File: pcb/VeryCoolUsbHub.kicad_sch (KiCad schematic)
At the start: 10 parts, among them U1 HC-USB3.0-L168-WP, U2 RTL8152B-VB-CG, U3 GL3510-OSY52, U4 HC-USB3.0-L168-WP

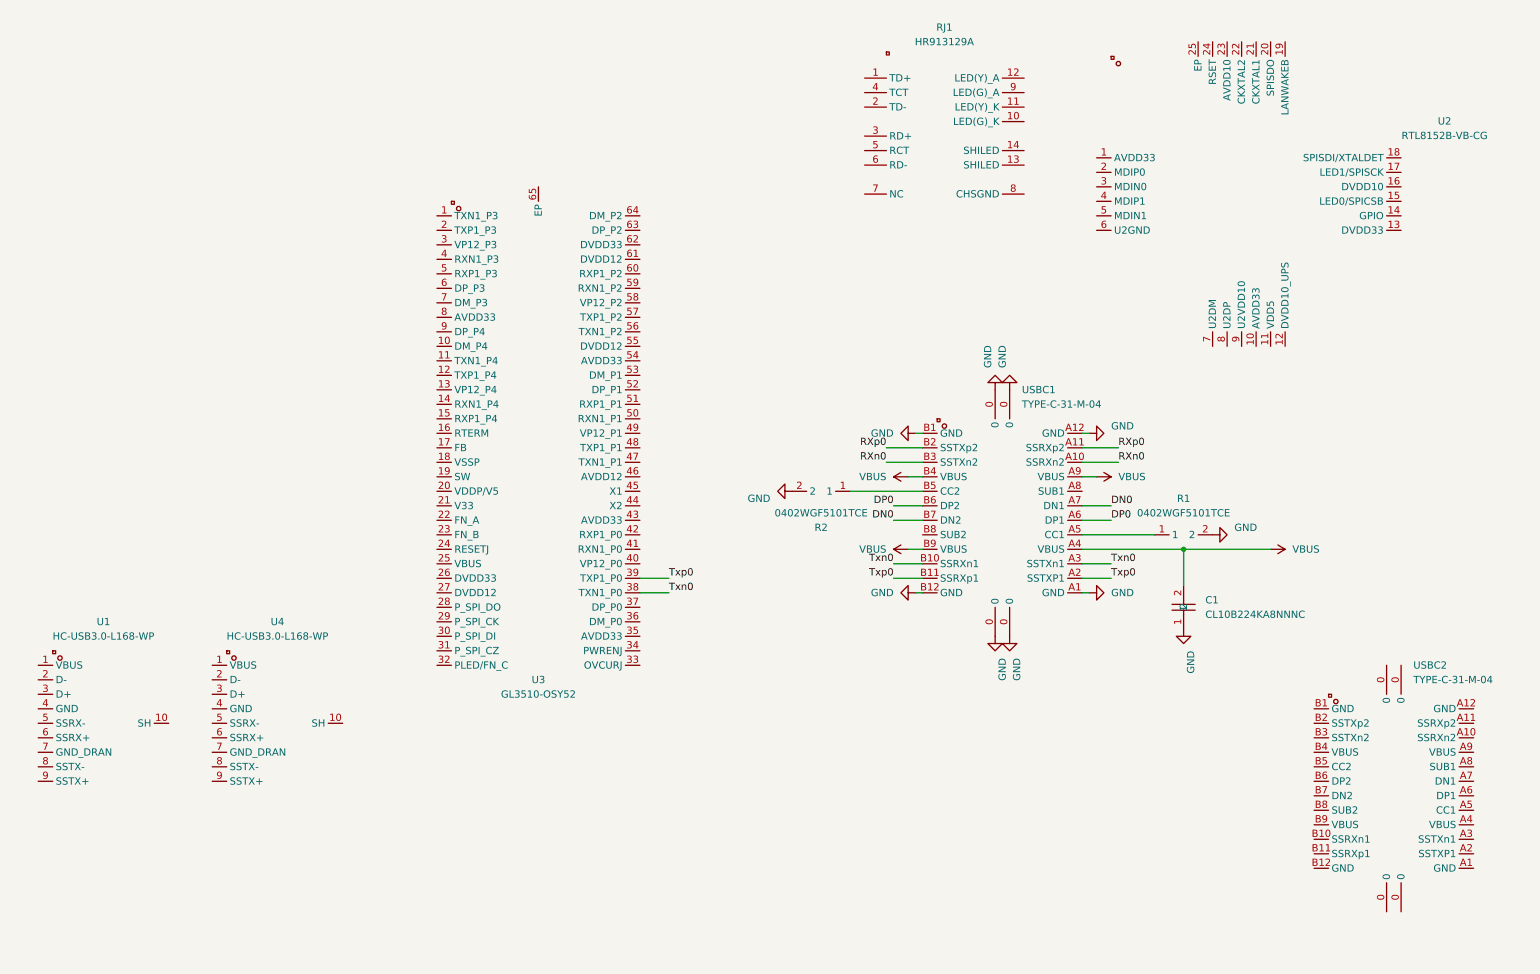
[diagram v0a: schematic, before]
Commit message: changed stuff, add schem for review
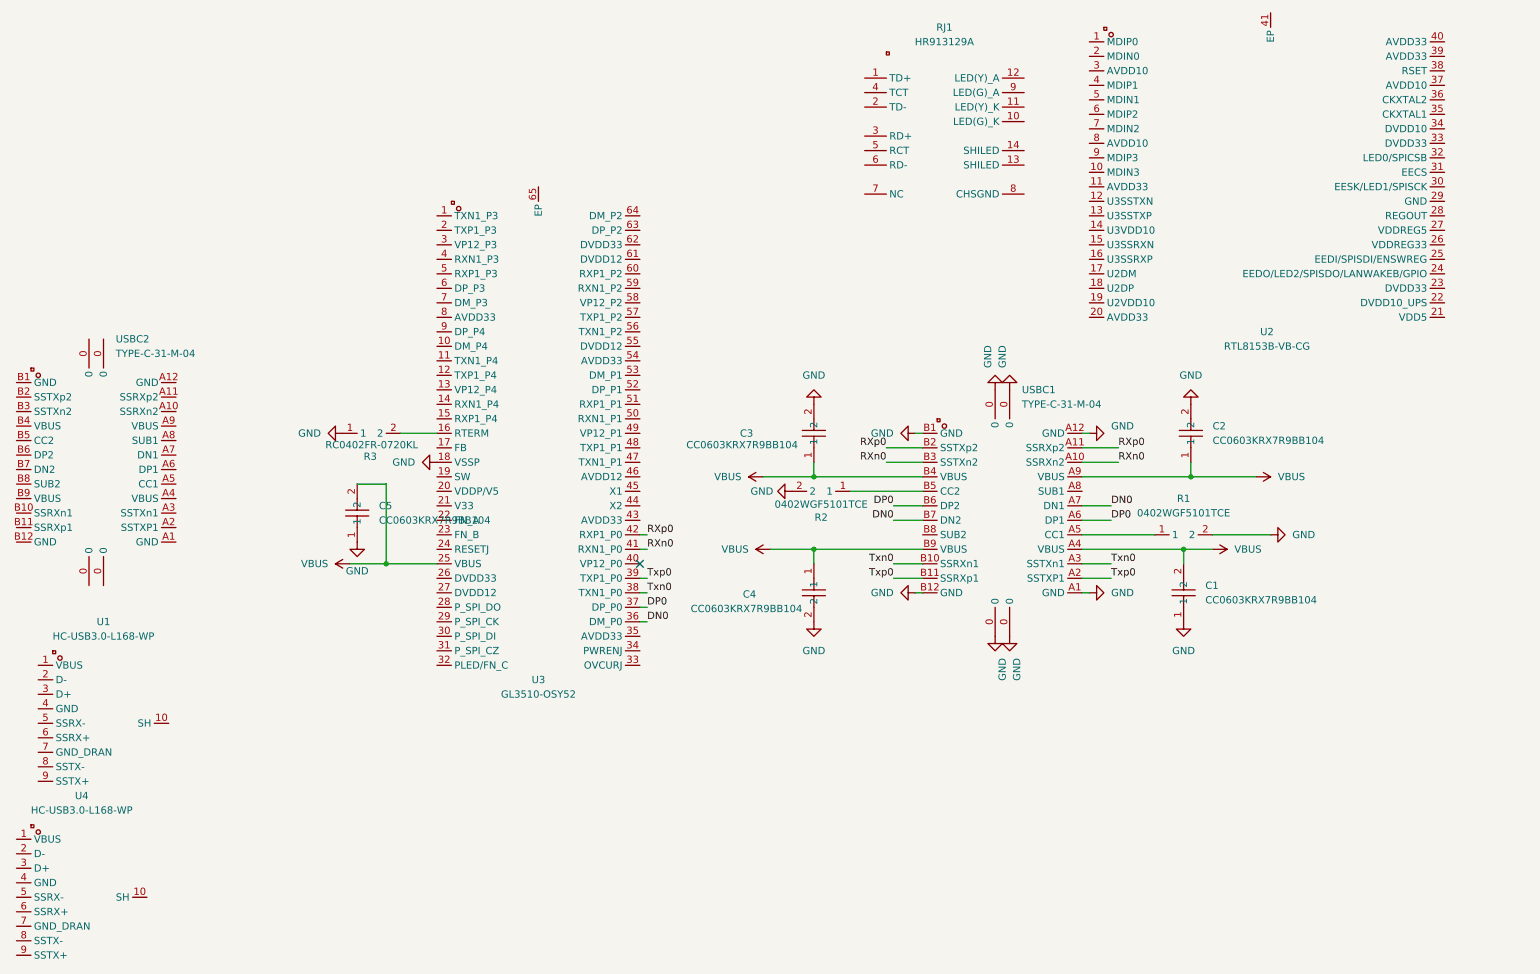
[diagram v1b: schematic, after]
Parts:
- removed C1: CL10B224KA8NNNC, EasyEDA:C0603, symbol EasyEDA:CL10B224KA8NNNC
- removed U2: RTL8152B-VB-CG, EasyEDA:QFN-24_L4.0-W4.0-P0.50-BL-EP2.0, symbol EasyEDA:RTL8152B-VB-CG
- added C1, C2, C3, C4, C5: CC0603KRX7R9BB104, EasyEDA:C0603, symbol EasyEDA:CC0603KRX7R9BB104
- added R3: RC0402FR-0720KL, EasyEDA:R0402, symbol EasyEDA:RC0402FR-0720KL
- added U2: RTL8153B-VB-CG, EasyEDA:QFN-40_L5.0-W5.0-P0.40-BL-EP3.7, symbol EasyEDA:RTL8153B-VB-CG
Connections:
- net DN0: now also U3.36 (DM_P0)
- net DP0: now also U3.37 (DP_P0)
- net GND: now also U3.18 (VSSP), C1.1, C2.2, C3.2, C4.2, C5.1, R3.1
- net RXn0: now also U3.41 (RXN1_P0)
- net RXp0: now also U3.42 (RXP1_P0)
- net VBUS: now also U3.25 (VBUS), C1.2, C2.1, C3.1, C4.1, C5.2
- net at U3.16 (RTERM): now also R3.2
- no-connect marks 0 -> 1
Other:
- moved on the sheet: U4, USBC2

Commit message: now with everything ig?
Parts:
- added C10, C11: CC0603KRX7R9BB104, EasyEDA:C0603, symbol EasyEDA:CC0603KRX7R9BB104
- added C6, C7: CC0603JRNPO9BN390, EasyEDA:C0603, symbol EasyEDA:CC0603JRNPO9BN390
- added C9: CL10A106KP8NNNC, EasyEDA:C0603, symbol EasyEDA:CL10A106KP8NNNC
- added X1: X322525MSB4SI, EasyEDA:CRYSTAL-SMD_4P-L3.2-W2.5-BL-2, symbol EasyEDA:X322525MSB4SI
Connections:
- net GND: now also C5.2, U1.10 (SH), U1.4 (GND), U1.7 (GND_DRAN), U4.10 (SH), U4.4 (GND), U4.7 (GND_DRAN), USBC2.0, USBC2.A1 (GND), USBC2.A12 (GND), USBC2.B1 (GND), USBC2.B12 (GND), C10.2, C11.2, C6.1, C7.2, C9.2, X1.2 (GND), X1.4 (GND); no longer C5.1
- net VBUS: now also C5.1, U1.1 (VBUS), U4.1 (VBUS), C10.1, C11.1, C9.1; no longer C5.2
- net at U2.35 (CKXTAL1): now also C6.2, X1.1 (OSC1)
- net at U2.36 (CKXTAL2): now also C7.1, X1.3 (OSC2)
- net DN1: now reaches U1.2 (D-)
- net DN1: now also U3.53 (DM_P1)
- net DP1: now reaches U1.3 (D+)
- net DP1: now also U3.52 (DP_P1)
- net RXn1: now reaches U1.5 (SSRX-)
- net RXn1: now also U3.50 (RXN1_P1)
- net RXp1: now reaches U1.6 (SSRX+)
- net RXp1: now also U3.51 (RXP1_P1)
- net Txn1: now reaches U1.8 (SSTX-)
- net Txn1: now also U3.47 (TXN1_P1)
- net Txp1: now reaches U1.9 (SSTX+)
- net Txp1: now also U3.48 (TXP1_P1)
- net Txn3: now reaches U3.1 (TXN1_P3)
- net Txp3: now reaches U3.2 (TXP1_P3)
- net RXn3: now reaches U3.4 (RXN1_P3)
- net RXp3: now reaches U3.5 (RXP1_P3)
- net Txn2: now reaches U3.56 (TXN1_P2)
- net Txn2: now also U4.8 (SSTX-)
- net Txp2: now reaches U3.57 (TXP1_P2)
- net Txp2: now also U4.9 (SSTX+)
- net RXn2: now reaches U3.59 (RXN1_P2)
- net RXn2: now also U4.5 (SSRX-)
- net DP3: now reaches U3.6 (DP_P3)
- net RXp2: now reaches U3.60 (RXP1_P2)
- net RXp2: now also U4.6 (SSRX+)
- net DP2: now reaches U3.63 (DP_P2)
- net DP2: now also U4.3 (D+)
- net DN2: now reaches U3.64 (DM_P2)
- net DN2: now also U4.2 (D-)
- net DN3: now reaches U3.7 (DM_P3)
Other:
- moved on the sheet: C1, C2, C3, C4, C5, R1, R2, RJ1, U1, U2, U4, USBC1

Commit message: done schem please
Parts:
- removed RJ1: HR913129A, EasyEDA:RJ45-TH_HR913129A, symbol EasyEDA:HR913129A
- added C12, C13, C14, C15, C16, C17, C8: CC0603KRX7R9BB104, EasyEDA:C0603, symbol EasyEDA:CC0603KRX7R9BB104
- added C18: CC0603JRNPO9BN390, EasyEDA:C0603, symbol EasyEDA:CC0603JRNPO9BN390
- added R4, R5: 0402WGF5602TCE, EasyEDA:R0402, symbol EasyEDA:0402WGF5602TCE
- added R6: RC0402FR-071KL, EasyEDA:R0402, symbol EasyEDA:RC0402FR-071KL
- added RJ45: HR911130A, EasyEDA:RJ45-TH_HR911130A, symbol EasyEDA:HR911130A
- added X2: X322525MSB4SI, EasyEDA:CRYSTAL-SMD_4P-L3.2-W2.5-BL-2, symbol EasyEDA:X322525MSB4SI
- renumbered USBC1 to USBC_IN, USBC2 to USBC_OUT, U1 to USB_OUT1, U4 to USB_OUT2
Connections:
- net DN3: now also U2.17 (U2DM), USBC_OUT.A7 (DN1)
- net DP3: now also USBC_OUT.A6 (DP1)
- net GND: now also C1.2, C2.1, C4.1, R1.1, U2.29 (GND), C12.1, C13.2, C14.1, C15.1, C16.2, C17.2, C18.1, C8.2, X2.2 (GND), X2.4 (GND); no longer C1.1, C2.2, C4.2, R1.2, USBC_IN.0, USBC_OUT.0, USB_OUT1.10 (SH), USB_OUT2.10 (SH)
- net RXn0: now also USBC_IN.B10 (SSRXn1); no longer USBC_IN.B3 (SSTXn2)
- net RXn3: now also USBC_OUT.A10 (SSRXn2)
- net RXp0: now also USBC_IN.B11 (SSRXp1); no longer USBC_IN.B2 (SSTXp2)
- net RXp3: now also USBC_OUT.A11 (SSRXp2)
- net Txn0: now also USBC_IN.B3 (SSTXn2); no longer USBC_IN.B10 (SSRXn1)
- net Txn3: now also USBC_OUT.A3 (SSTXn1)
- net Txp0: now also USBC_IN.B2 (SSTXp2); no longer USBC_IN.B11 (SSRXp1)
- net Txp3: now also USBC_OUT.A2 (SSTXP1)
- net VBUS: now also C1.1, C2.2, C4.2, U2.21 (VDD5), U2.27 (VDDREG5), U3.20 (VDDP/V5), USBC_OUT.A9 (VBUS), C13.1, C16.1, C17.1, C8.1, R4.2, R5.2; no longer C1.2, C2.1, C4.1
- net MDIP0: now reaches U2.1 (MDIP0)
- net MDIP0: now also RJ45.P2 (MDI0+)
- net MDIN3: now reaches U2.10 (MDIN3)
- net MDIN3: now also RJ45.P9 (MDI3-)
- net Txn4: now reaches U2.12 (U3SSTXN)
- net Txn4: now also U3.11 (TXN1_P4)
- net Txp4: now reaches U2.13 (U3SSTXP)
- net Txp4: now also U3.12 (TXP1_P4)
- net RXn4: now reaches U2.15 (U3SSRXN)
- net RXn4: now also U3.14 (RXN1_P4)
- net RXp4: now reaches U2.16 (U3SSRXP)
- net RXp4: now also U3.15 (RXP1_P4)
- net DP4: now reaches U2.18 (U2DP)
- net DP4: now also U3.9 (DP_P4)
- net MDIN0: now reaches U2.2 (MDIN0)
- net MDIN0: now also RJ45.P3 (MDI0-)
- net V3.3: now reaches U2.23 (DVDD33)
- net V3.3: now also U2.26 (VDDREG33), U3.21 (V33), C14.2, C15.2, R6.2
- net LED2: now reaches U2.24 (EEDO/LED2/SPISDO/LANWAKEB/GPIO)
- net LED2: now also RJ45.13
- net LED1: now reaches U2.30 (EESK/LED1/SPISCK)
- net LED1: now also RJ45.12
- net MDIP1: now reaches U2.4 (MDIP1)
- net MDIP1: now also RJ45.P4 (MDI1+)
- net MDIN1: now reaches U2.5 (MDIN1)
- net MDIN1: now also RJ45.P7 (MDI1-)
- net MDIP2: now reaches U2.6 (MDIP2)
- net MDIP2: now also RJ45.P5 (MDI2+)
- net MDIN2: now reaches U2.7 (MDIN2)
- net MDIN2: now also RJ45.P6 (MDI2-)
- net MDIP3: now reaches U2.9 (MDIP3)
- net MDIP3: now also RJ45.P8 (MDI3+)
- net at USBC_IN.A5 (CC1): now also R1.2; no longer R1.1
- net DN4: now reaches U3.10 (DM_P4)
- net at U3.44 (X2): now also C18.2, X2.3 (OSC2)
- net at U3.45 (X1): now also X2.1 (OSC1)
- net at USBC_OUT.A5 (CC1): now also R4.1
- net at USBC_OUT.B5 (CC2): now also R5.1
- new net: C12.2, RJ45.P1
- new net: R6.1, RJ45.11, RJ45.14
- no-connect marks 1 -> 40
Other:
- moved on the sheet: C1, C10, C11, C2, C3, C4, C5, C6, C7, C9, R1, R2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

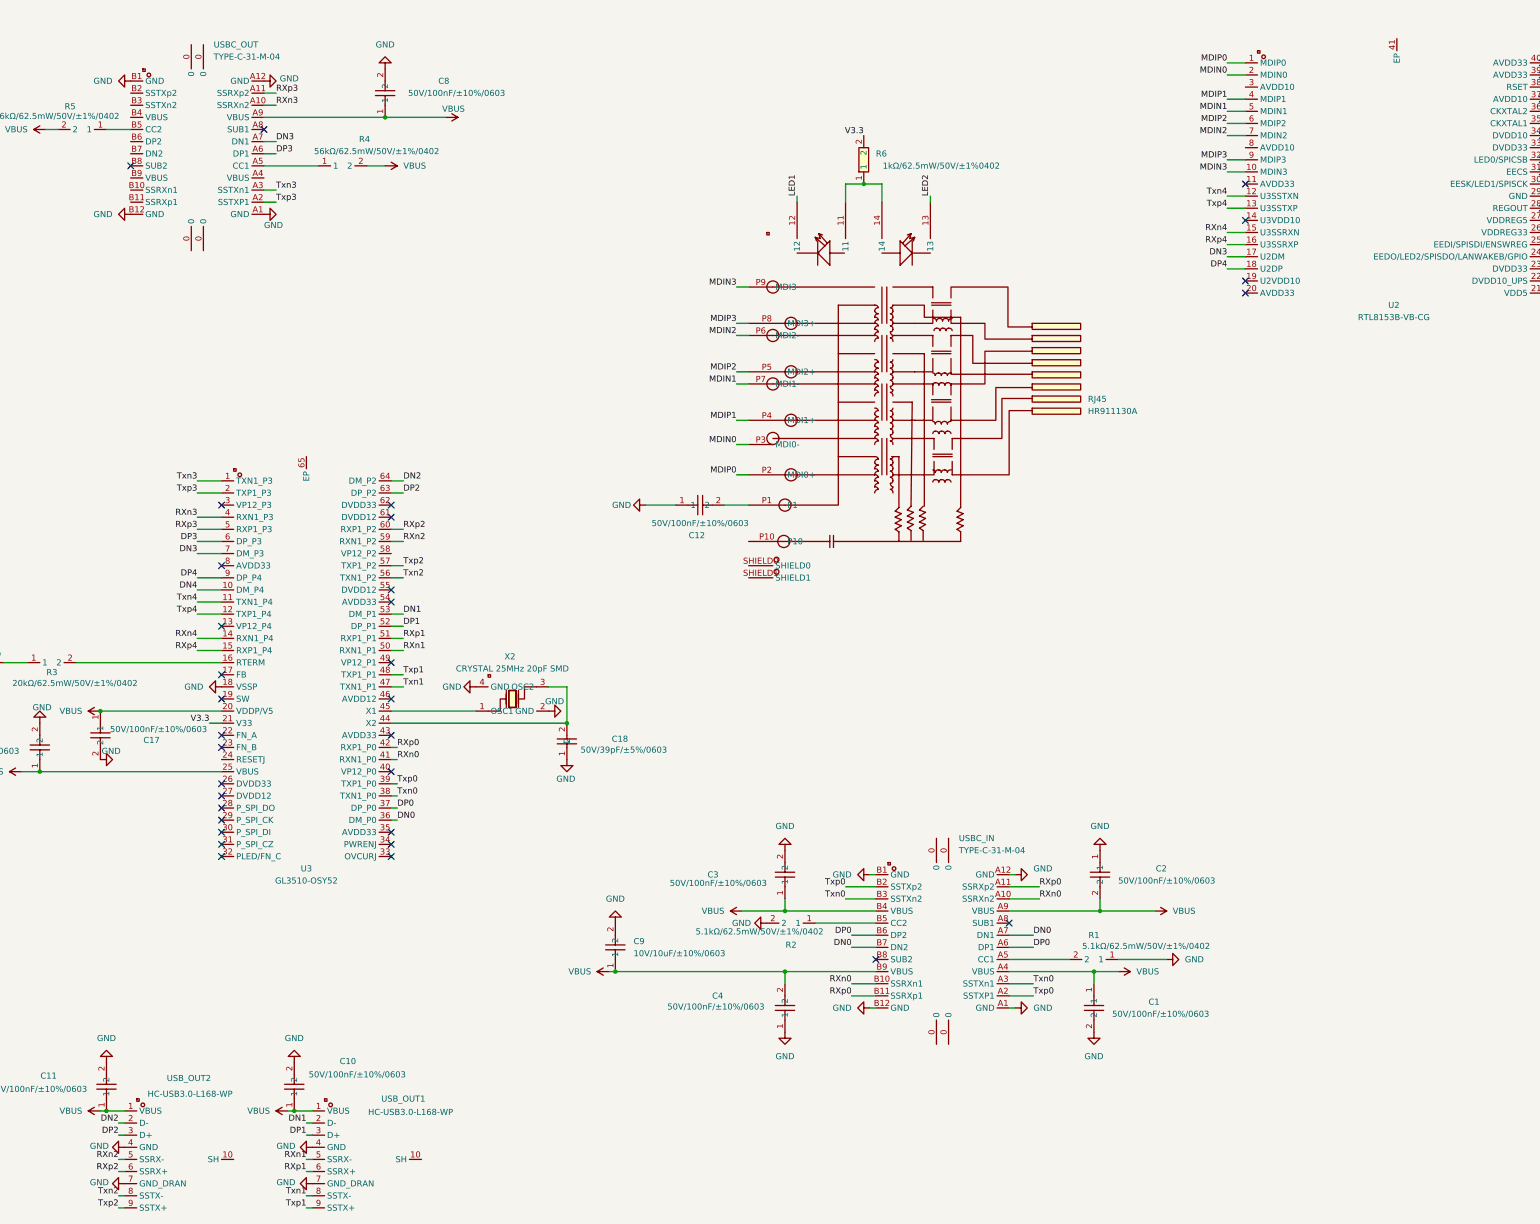
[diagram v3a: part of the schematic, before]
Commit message: forgor to link shield to ground
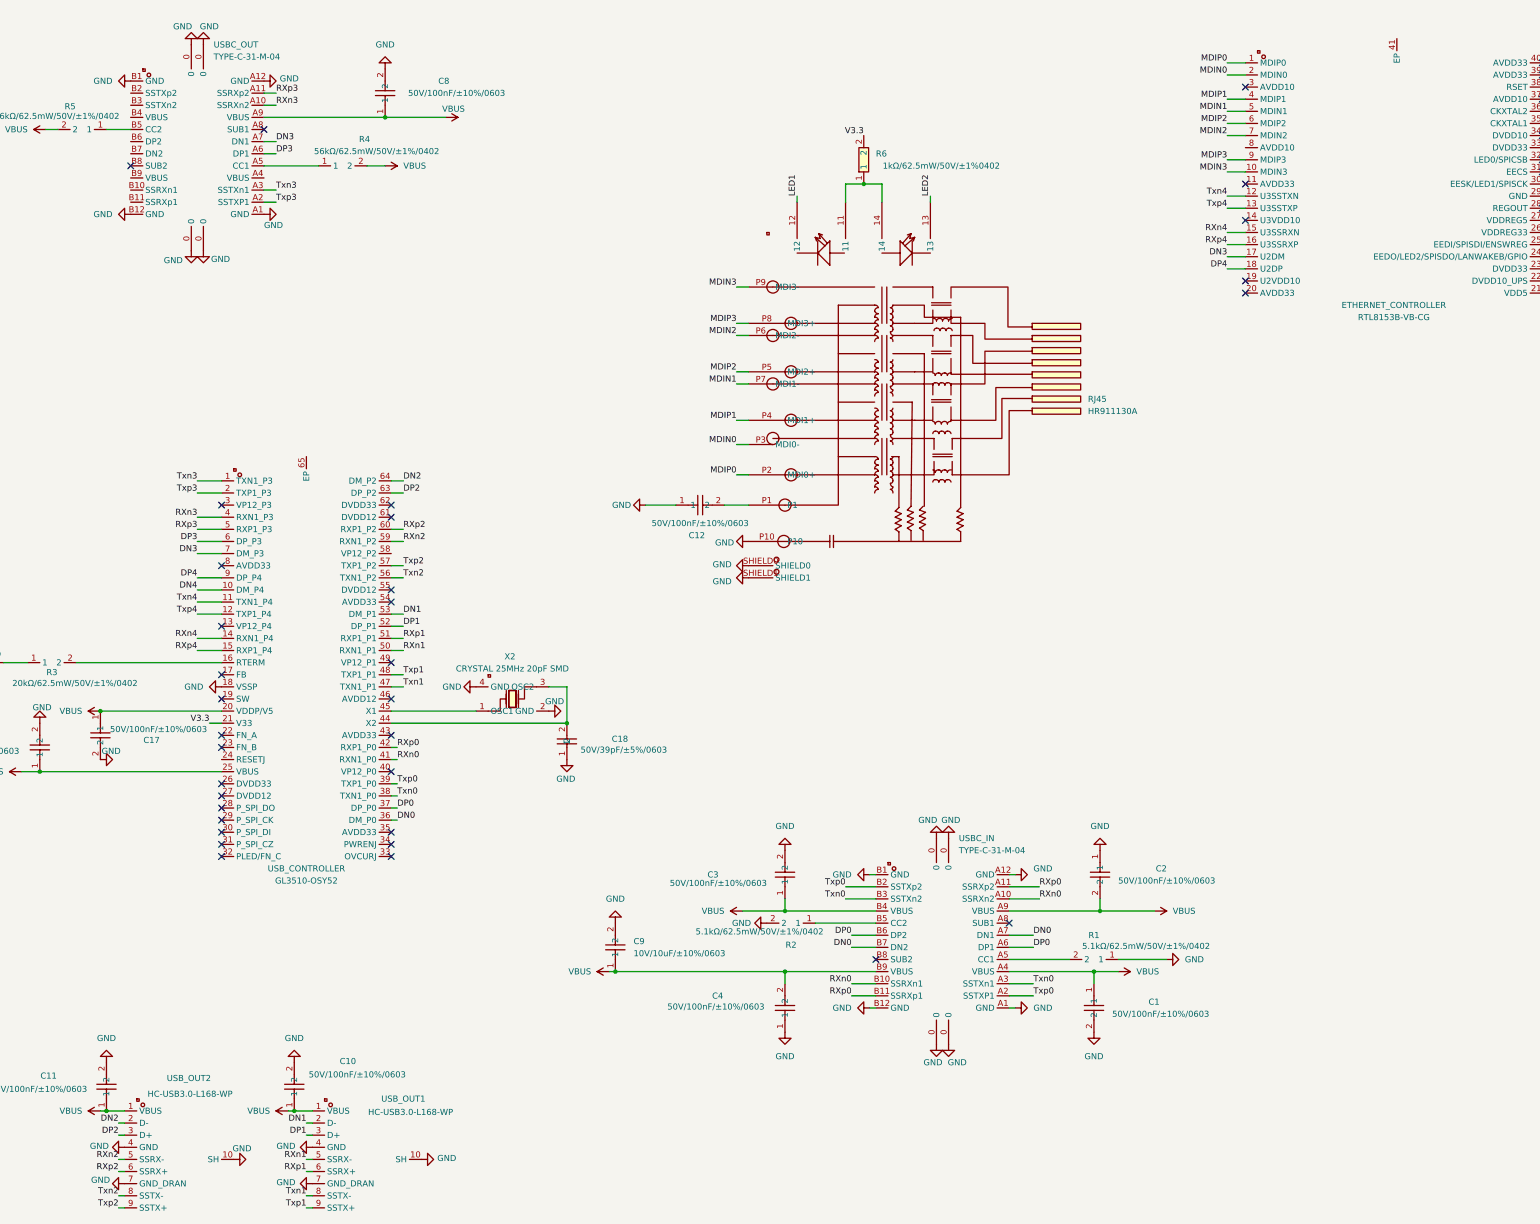
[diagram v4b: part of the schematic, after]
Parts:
- renumbered U2 to ETHERNET_CONTROLLER, U3 to USB_CONTROLLER
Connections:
- net GND: now also RJ45.P10, RJ45.SHIELD0, RJ45.SHIELD1, USBC_IN.0, USBC_OUT.0, USB_OUT1.10 (SH), USB_OUT2.10 (SH)
- no-connect marks 40 -> 41

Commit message: do sum pcb
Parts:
- renumbered ETHERNET_CONTROLLER to ETHERNET_CONTROLLER1, USBC_IN to USBC_IN1, USBC_OUT to USBC_OUT1, USB_CONTROLLER to USB_CONTROLLER1
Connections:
- no-connect marks 41 -> 43
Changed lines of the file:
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@@
 	)
 	(no_connect
+		(at 340.36 81.28)
+	)
+	(no_connect
 		(at 63.5 153.67)
 	)
@@
 	)
 	(no_connect
+		(at 278.13 53.34)
+	)
+	(no_connect
 		(at 99.06 146.05)
 	)
@@
 		(dnp no)
 		(fields_autoplaced yes)
-		(property "Reference" "ETHERNET_CONTROLLER"
+		(property "Reference" "ETHERNET_CONTROLLER1"
 			(at 309.245 86.36 0)
 			(effects
@@
 			(project ""
 				(path "/a66e963d-9223-4dd6-b11b-c5e7c640f212"
-					(reference "ETHERNET_CONTROLLER")
+					(reference "ETHERNET_CONTROLLER1")
 					(unit 1)
 				)
@@
 		(dnp no)
 		(fields_autoplaced yes)
-		(property "Reference" "USB_CONTROLLER"
+		(property "Reference" "USB_CONTROLLER1"
 			(at 81.28 204.47 0)
 			(effects
@@
 			(project ""
 				(path "/a66e963d-9223-4dd6-b11b-c5e7c640f212"
-					(reference "USB_CONTROLLER")
+					(reference "USB_CONTROLLER1")
 					(unit 1)
 				)
@@
 		(dnp no)
 		(fields_autoplaced yes)
-		(property "Reference" "USBC_IN"
+		(property "Reference" "USBC_IN1"
 			(at 218.0433 198.12 0)
 			(effects
@@
 			(project ""
 				(path "/a66e963d-9223-4dd6-b11b-c5e7c640f212"
-					(reference "USBC_IN")
+					(reference "USBC_IN1")
 					(unit 1)
 				)
@@
 		(dnp no)
 		(fields_autoplaced yes)
-		(property "Reference" "USBC_OUT"
+		(property "Reference" "USBC_OUT1"
 			(at 61.8333 31.75 0)
 			(effects
@@
 			(project "VeryCoolUsbHub"
 				(path "/a66e963d-9223-4dd6-b11b-c5e7c640f212"
-					(reference "USBC_OUT")
+					(reference "USBC_OUT1")
 					(unit 1)
 				)
